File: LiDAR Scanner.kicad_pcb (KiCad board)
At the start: 4 copper layers, 82 x 82 mm, 49 parts, among them J1 USB4215-03-A, J2 PWR TEST, J3 UART DEBUG, J4 GPIO DEBUG, J5 SWD, J6 GENERAL DEBUG, SW1 RESET, SW2 SW_Nidec_CAS-120A1, U2 ICM-42688-P, U3 AP2112K-3.3, U4 USBLC6-2SC6, U5 STM32F411CEUx, Y1 8MHz

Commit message: Finalized board + gerbers
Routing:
- net GND: vias 191 -> 183

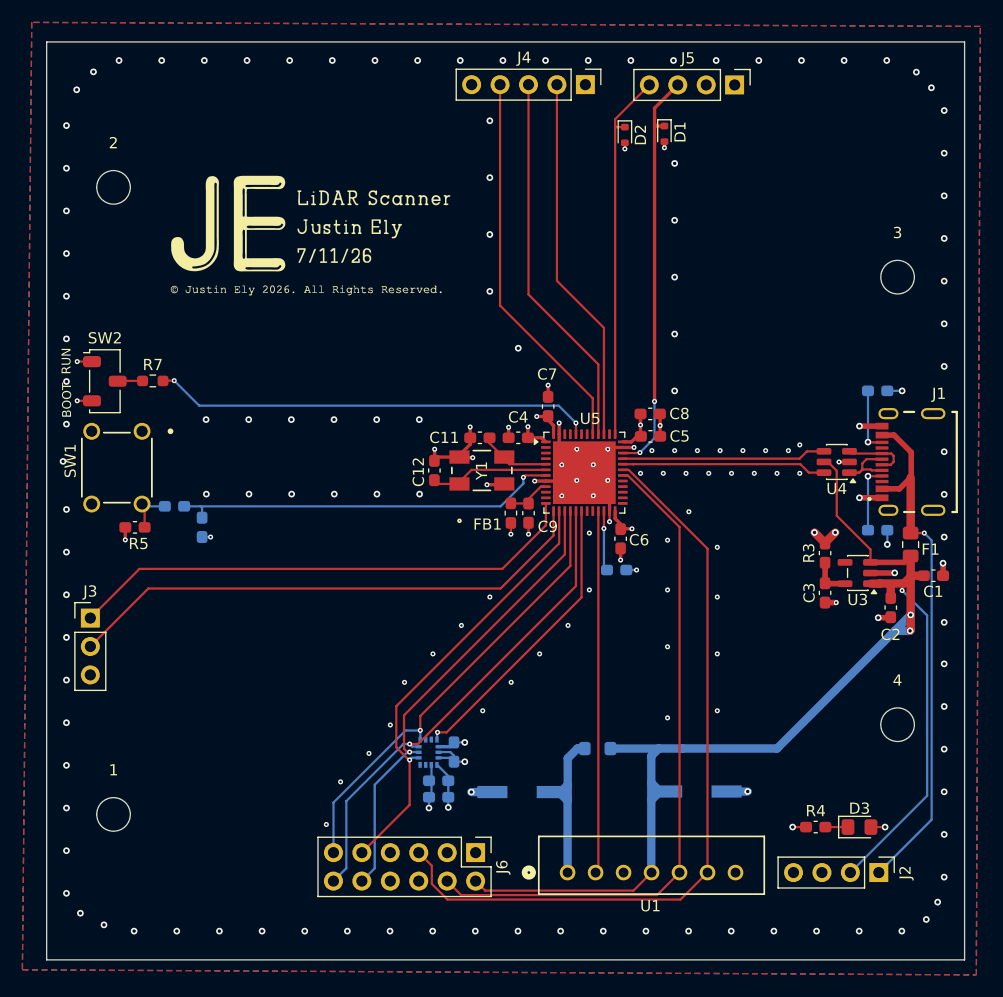
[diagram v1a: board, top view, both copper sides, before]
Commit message: fixed stitching vias
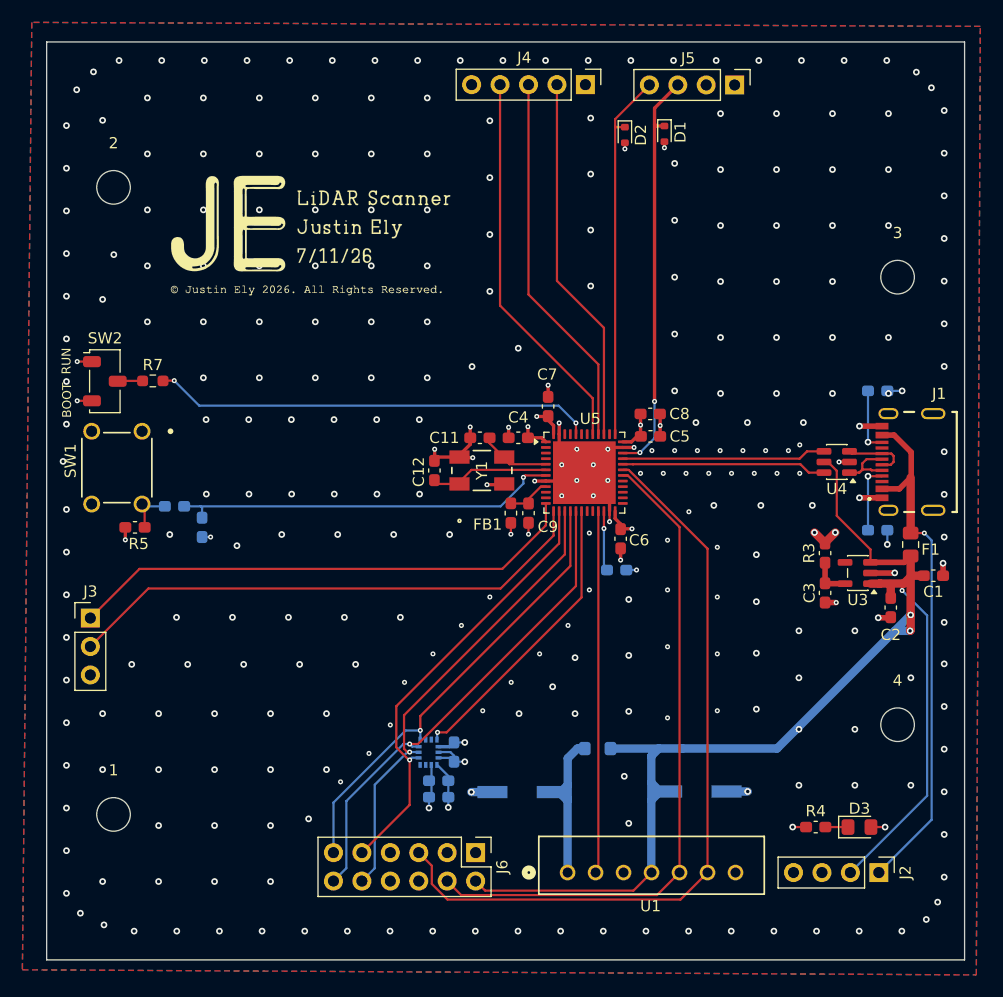
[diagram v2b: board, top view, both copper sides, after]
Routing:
- net GND: vias 183 -> 311
